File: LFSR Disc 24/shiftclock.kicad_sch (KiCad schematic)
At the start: 8 parts, among them U801 LM555xN

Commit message: Board layout and schematic tweaks
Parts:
- U801: footprint Package_DIP:DIP-8_W7.62mm -> Package_DIP:DIP-8_W7.62mm_Socket
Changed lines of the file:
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@@
       (effects (font (size 1.27 1.27)))
     )
-    (property "Footprint" "Package_DIP:DIP-8_W7.62mm" (at 135.89 91.44 0)
+    (property "Footprint" "Package_DIP:DIP-8_W7.62mm_Socket" (at 135.89 91.44 0)
       (effects (font (size 1.27 1.27)) hide)
     )

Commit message: Final routing
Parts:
- removed C801: 10u, Capacitor_THT:CP_Radial_D4.0mm_P1.50mm, symbol LFSR Logo-rescue:CP-Device
- added C401: C_Polarized_Small, Capacitor_THT:CP_Radial_D4.0mm_P1.50mm, symbol Device:C_Polarized_Small
- added J102: Conn_01x02_Pin, Connector_PinHeader_2.54mm:PinHeader_1x02_P2.54mm_Vertical, symbol Connector:Conn_01x02_Pin
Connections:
- net +5V: now also R801.2; no longer R801.1
- net CLK: now also J102.2 (Pin_2)
- net DIVIDER: now also R801.1; no longer R801.2
- net GND: now also C401.2, J102.1 (Pin_1)
- net TRTHR: now also RV401.1, C401.1; no longer RV401.3
- net at R802.2: now also RV401.3; no longer RV401.1
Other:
- moved on the sheet: R801

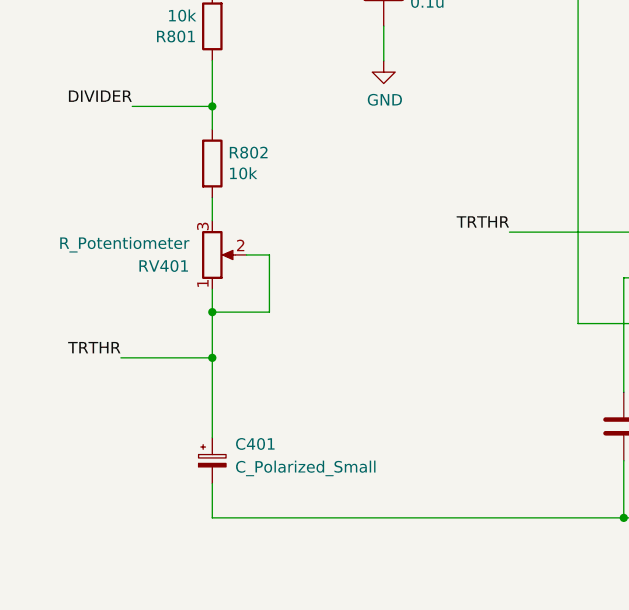
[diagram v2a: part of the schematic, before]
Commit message: Update some values
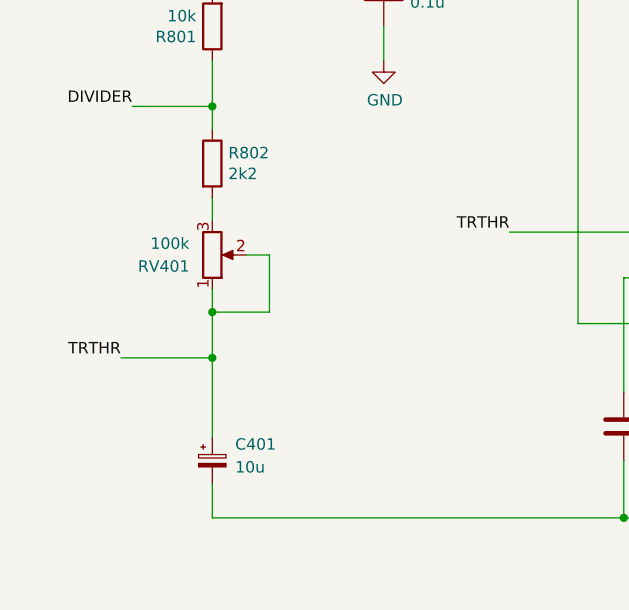
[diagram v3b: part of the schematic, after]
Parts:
- C401: value C_Polarized_Small -> 10u
- R802: value 10k -> 2k2
- RV401: value R_Potentiometer -> 100k
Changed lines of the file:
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@@
       (effects (font (size 1.27 1.27)) (justify left))
     )
-    (property "Value" "C_Polarized_Small" (at 55.88 102.3239 0)
+    (property "Value" "10u" (at 55.88 102.3239 0)
       (effects (font (size 1.27 1.27)) (justify left))
     )
@@
       (effects (font (size 1.27 1.27)) (justify right))
     )
-    (property "Value" "R_Potentiometer" (at 50.8 77.47 0)
+    (property "Value" "100k" (at 50.8 77.47 0)
       (effects (font (size 1.27 1.27)) (justify right))
     )
@@
       (effects (font (size 1.27 1.27)) (justify left))
     )
-    (property "Value" "10k" (at 55.118 69.723 0)
-      (effects (font (size 1.27 1.27)) (justify left))
-    )
+    (property "Value" "2k2" (at 55.118 69.723 0)
+      (effects (font (size 1.27 1.27)) (justify left))
+    )
